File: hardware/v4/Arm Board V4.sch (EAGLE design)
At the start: 35 parts, among them IC1 4503D, IC2 4503D, IC7 7812DT, IC9 7812DT, Q3 Q_LTC490, U2 XBEE-1B3

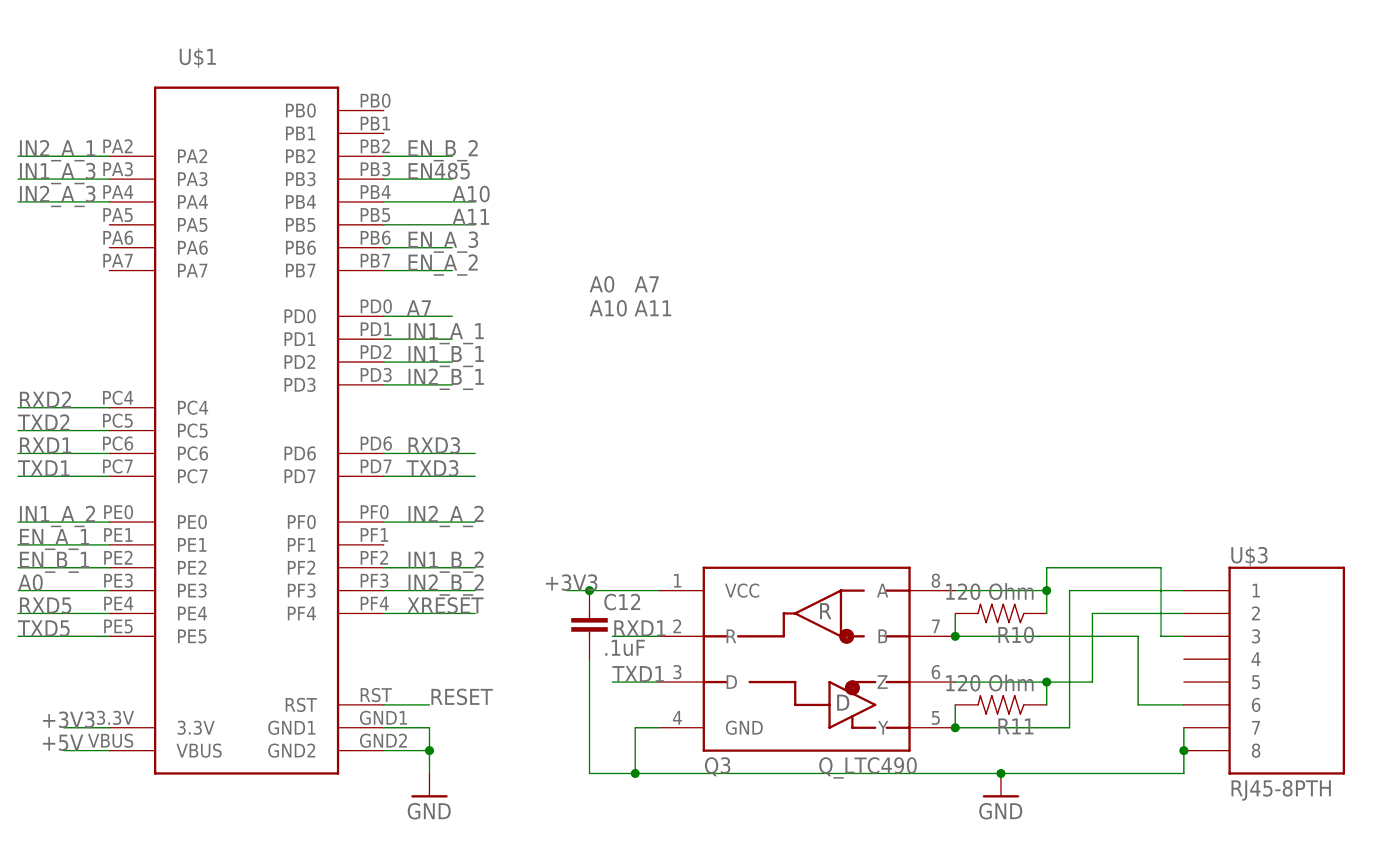
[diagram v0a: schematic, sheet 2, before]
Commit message: Continued work on V4
Started to route power and fixed inconsistency
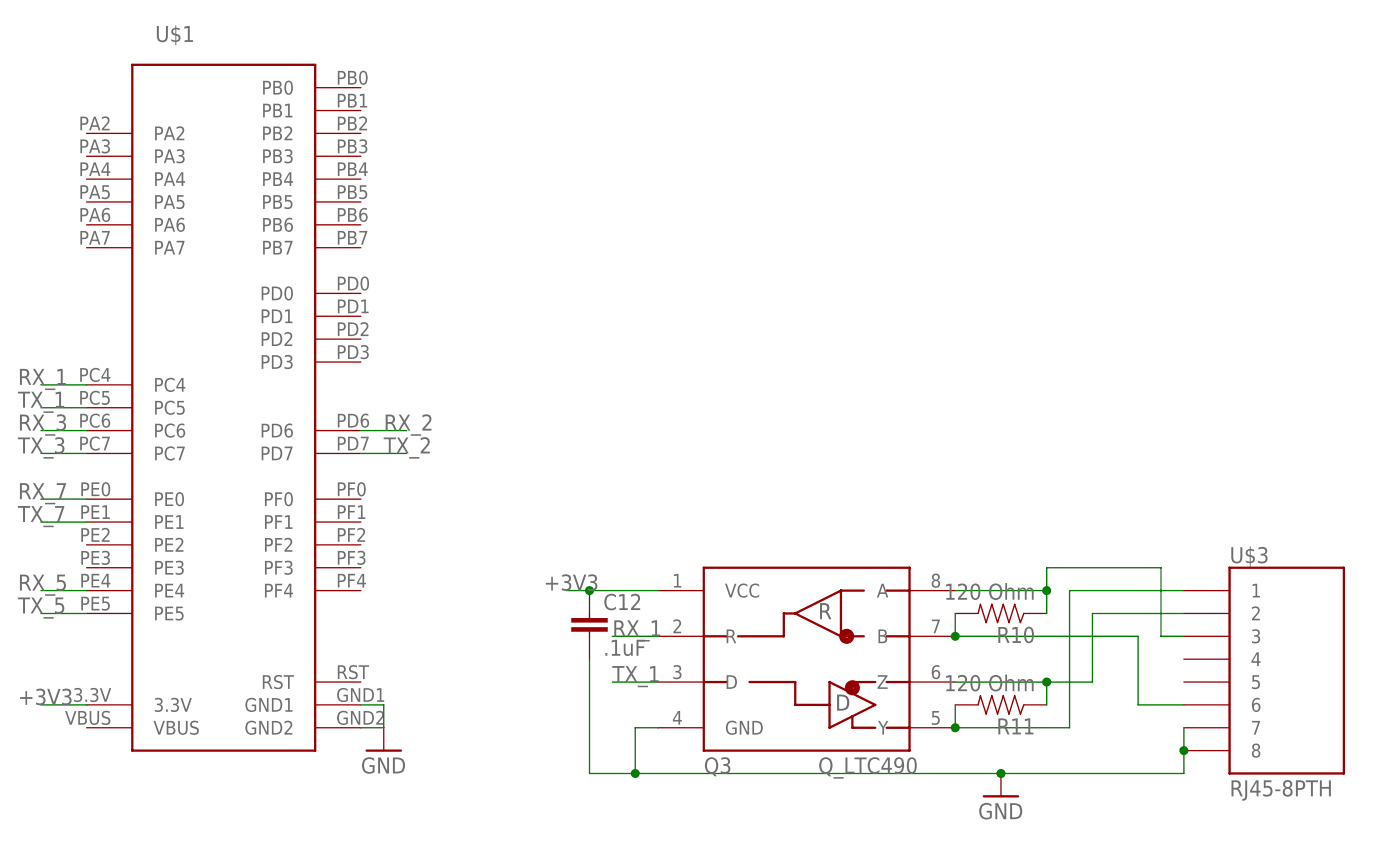
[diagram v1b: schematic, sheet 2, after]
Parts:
- C12: device SparkFun-Capacitors:0.1UF-25V-5%(0603) -> SparkFun-Capacitors:2.2UF-CERCAP-10009
- C20, C21, C22, C23: value 0.1uF -> .1uF; device SparkFun-Capacitors:0.1UF-25V(+80/-20%)(0603) -> SparkFun-Capacitors:2.2UF-CERCAP-10009
- R10, R11: device SparkFun-Passives:RESISTOR0603-RES -> SparkFun-Passives:RESISTOR1206
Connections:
- net EN_A_1 renamed TX_7
- net IN1_A_2 renamed RX_7
- net RXD5 renamed RX_5
- net TXD5 renamed TX_5
- removed net A0: U$1.PE3
- removed net A10: U$1.PB4
- removed net A11: U$1.PB5
- removed net A7: U$1.PD0
- removed net EN485: U$1.PB3
- removed net EN_A_2: U$1.PB7
- removed net EN_A_3: U$1.PB6
- removed net EN_B_1: U$1.PE2
- removed net EN_B_2: U$1.PB2
- removed net IN1_A_1: U$1.PD1
- removed net IN1_A_3: U$1.PA3
- removed net IN1_B_1: U$1.PD2
- removed net IN1_B_2: U$1.PF2
- removed net IN2_A_1: U$1.PA2
- removed net IN2_A_2: U$1.PF0
- removed net IN2_A_3: U$1.PA4
- removed net IN2_B_1: U$1.PD3
- removed net IN2_B_2: U$1.PF3
- removed net RESET: U$1.RST
- removed net RXD1: Q3.R, U$1.PC6
- removed net RXD2: U$1.PC4
- removed net TXD1: Q3.D, U$1.PC7
- removed net TXD2: U$1.PC5
- new net RX_1: Q3.R, U$1.PC4
- new net RX_2: U$1.PD6
- new net RX_3: U$1.PC6
- new net TX_1: Q3.D, U$1.PC5
- new net TX_2: U$1.PD7
- new net TX_3: U$1.PC7
- net +5V: no longer U$1.VBUS
- net RXD3: no longer U$1.PD6
- net TXD3: no longer U$1.PD7
- net XRESET: no longer U$1.PF4
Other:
- note removed: "A0 A7 A10 A11"
- moved on the sheet: U$1

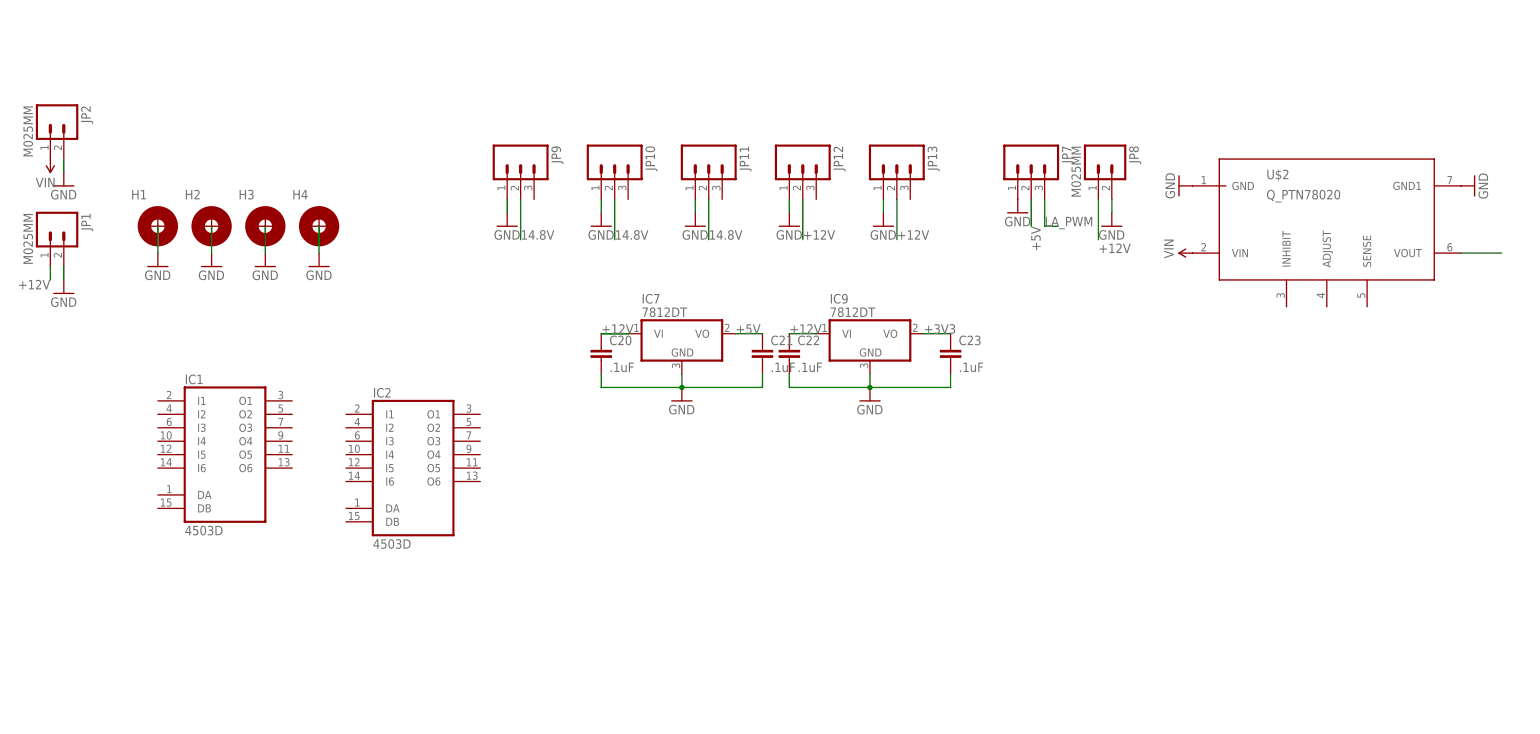
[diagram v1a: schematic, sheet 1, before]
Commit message: Router power and data lines and assigned pins
Started to route more of the data lines to where they will go.  As well
as working on assigning pins to components.
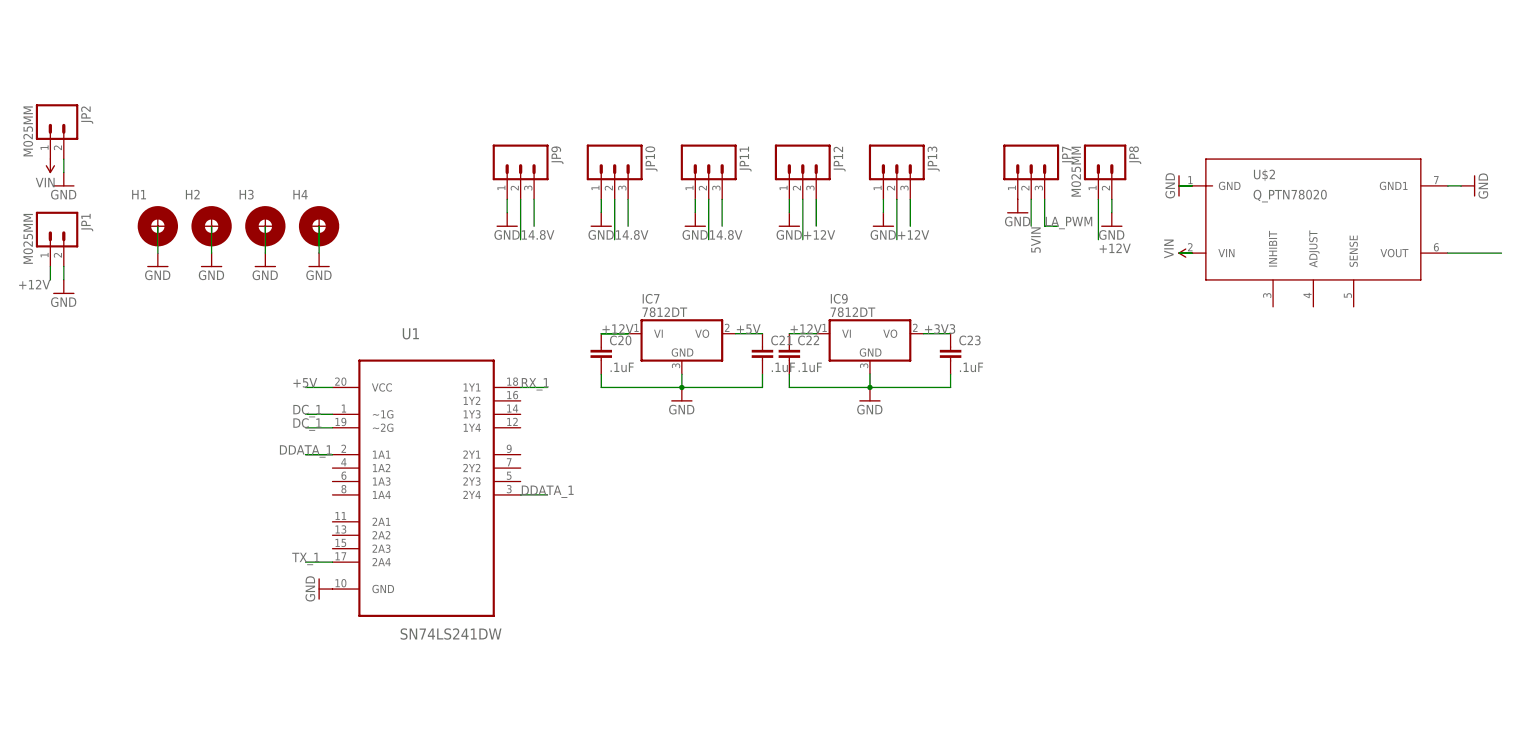
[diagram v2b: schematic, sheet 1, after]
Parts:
- removed IC1, IC2: 4503D, 45xx:4503D
- added U1: SN74LS241DW, 74LS241:SN74LS241DW
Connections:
- removed net RXD3: LED2.C, U2.DOUT
- removed net TXD3: LED3.C, U2.DIN
- new net 5VIN: JP7.2
- new net DC_1: U$1.PB3, U1.~1G, U1.~2G
- new net DDATA_1: JP10.3, JP11.3, JP12.3, JP13.3, JP9.3, U1.1A1, U1.2Y4
- net +5V: now also U1.VCC; no longer JP7.2
- net GND: now also U1.GND
- net LA_PWM: now also U$1.PB6
- net RX_1: now also U1.1Y1; no longer Q3.R
- net RX_2: now also Q3.R
- net RX_3: now also LED2.C, U2.DOUT
- net TX_1: now also U1.2A4; no longer Q3.D
- net TX_2: now also Q3.D
- net TX_3: now also LED3.C, U2.DIN
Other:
- moved on the sheet: U$2

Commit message: Added a few things and cleaned up some stuff
Added a few things from last night but mostly cleaning up traces and
adding parts to it.  Commit message last night was by Seto so ignore the
message.
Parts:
- added JP4, JP5: (no value), SparkFun-Connectors:M041X04_NO_SILK
- added Q1, Q2, Q4: MOSFET-NCHANNELFQP30N06L, SparkFun-DiscreteSemi:MOSFET-NCHANNELFQP30N06L
- added R3, R6, R7: 150, SparkFun-Passives:RESISTOR1206
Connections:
- new net O1: JP4.2, JP5.2, Q1.D
- new net O2: JP4.3, JP5.3, Q2.D
- new net O3: JP4.4, JP5.4, Q4.D
- new net PWM1: Q1.G, R3.2, U$1.PD1
- new net PWM2: Q2.G, R6.2, U$1.PD2
- new net PWM3: Q4.G, R7.2, U$1.PD3
- net +12V: now also JP4.1, JP5.1
- net GND: now also Q1.S, Q2.S, Q4.S, R3.1, R6.1, R7.1
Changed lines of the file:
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@@
 <part name="U1" library="74LS241" deviceset="SN74LS241DW" device=""/>
 <part name="GND18" library="SparkFun-Aesthetics" deviceset="GND" device=""/>
+<part name="Q1" library="SparkFun-DiscreteSemi" deviceset="MOSFET-NCHANNEL" device="FQP30N06L"/>
+<part name="R3" library="SparkFun-Passives" deviceset="RESISTOR" device="1206" value="150"/>
+<part name="U$4" library="Lib_Documentation" deviceset="SUP_GND" device=""/>
+<part name="Q2" library="SparkFun-DiscreteSemi" deviceset="MOSFET-NCHANNEL" device="FQP30N06L"/>
+<part name="R6" library="SparkFun-Passives" deviceset="RESISTOR" device="1206" value="150"/>
+<part name="U$5" library="Lib_Documentation" deviceset="SUP_GND" device=""/>
+<part name="Q4" library="SparkFun-DiscreteSemi" deviceset="MOSFET-NCHANNEL" device="FQP30N06L"/>
+<part name="R7" library="SparkFun-Passives" deviceset="RESISTOR" device="1206" value="150"/>
+<part name="U$6" library="Lib_Documentation" deviceset="SUP_GND" device=""/>
+<part name="JP4" library="SparkFun-Connectors" deviceset="M04" device="1X04_NO_SILK"/>
+<part name="JP5" library="SparkFun-Connectors" deviceset="M04" device="1X04_NO_SILK"/>
 </parts>
 <sheets>
@@
 <instance part="U1" gate="A" x="76.2" y="-7.62"/>
 <instance part="GND18" gate="1" x="55.88" y="-30.48" rot="R270"/>
+<instance part="Q1" gate="G$1" x="208.28" y="0"/>
+<instance part="R3" gate="G$1" x="195.58" y="-5.08" rot="R90"/>
+<instance part="U$4" gate="G$1" x="200.66" y="-5.08" rot="R180"/>
+<instance part="Q2" gate="G$1" x="208.28" y="-22.86"/>
+<instance part="R6" gate="G$1" x="195.58" y="-27.94" rot="R90"/>
+<instance part="U$5" gate="G$1" x="200.66" y="-27.94" rot="R180"/>
+<instance part="Q4" gate="G$1" x="208.28" y="-45.72"/>
+<instance part="R7" gate="G$1" x="195.58" y="-50.8" rot="R90"/>
+<instance part="U$6" gate="G$1" x="200.66" y="-50.8" rot="R180"/>
+<instance part="JP4" gate="G$1" x="279.4" y="-2.54" rot="R180"/>
+<instance part="JP5" gate="G$1" x="279.4" y="-22.86" rot="R180"/>
 </instances>
 <busses>
@@
 <pinref part="GND18" gate="1" pin="GND"/>
 </segment>
+<segment>
+<pinref part="R3" gate="G$1" pin="1"/>
+<pinref part="Q1" gate="G$1" pin="S"/>
+<wire x1="208.28" y1="-5.08" x2="208.28" y2="-10.16" width="0.1524" layer="91"/>
+<wire x1="208.28" y1="-10.16" x2="200.66" y2="-10.16" width="0.1524" layer="91"/>
+<pinref part="U$4" gate="G$1" pin="GND"/>
+<wire x1="200.66" y1="-10.16" x2="195.58" y2="-10.16" width="0.1524" layer="91"/>
+<wire x1="200.66" y1="-7.62" x2="200.66" y2="-10.16" width="0.1524" layer="91"/>
+</segment>
+<segment>
+<pinref part="R6" gate="G$1" pin="1"/>
+<pinref part="Q2" gate="G$1" pin="S"/>
+<wire x1="208.28" y1="-27.94" x2="208.28" y2="-33.02" width="0.1524" layer="91"/>
+<wire x1="208.28" y1="-33.02" x2="200.66" y2="-33.02" width="0.1524" layer="91"/>
+<pinref part="U$5" gate="G$1" pin="GND"/>
+<wire x1="200.66" y1="-33.02" x2="195.58" y2="-33.02" width="0.1524" layer="91"/>
+<wire x1="200.66" y1="-30.48" x2="200.66" y2="-33.02" width="0.1524" layer="91"/>
+</segment>
+<segment>
+<pinref part="R7" gate="G$1" pin="1"/>
+<pinref part="Q4" gate="G$1" pin="S"/>
+<wire x1="208.28" y1="-50.8" x2="208.28" y2="-55.88" width="0.1524" layer="91"/>
+<wire x1="208.28" y1="-55.88" x2="200.66" y2="-55.88" width="0.1524" layer="91"/>
+<pinref part="U$6" gate="G$1" pin="GND"/>
+<wire x1="200.66" y1="-55.88" x2="195.58" y2="-55.88" width="0.1524" layer="91"/>
+<wire x1="200.66" y1="-53.34" x2="200.66" y2="-55.88" width="0.1524" layer="91"/>
+</segment>
 </net>
 <net name="+12V" class="0">
@@
 <pinref part="JP12" gate="G$1" pin="2"/>
 </segment>
+<segment>
+<pinref part="JP4" gate="G$1" pin="1"/>
+<wire x1="274.32" y1="0" x2="269.24" y2="0" width="0.1524" layer="91"/>
+<label x="269.24" y="0" size="1.778" layer="95"/>
+</segment>
+<segment>
+<pinref part="JP5" gate="G$1" pin="1"/>
+<wire x1="274.32" y1="-20.32" x2="269.24" y2="-20.32" width="0.1524" layer="91"/>
+<label x="269.24" y="-20.32" size="1.778" layer="95"/>
+</segment>
 </net>
 <net name="+5V" class="0">
@@
 <wire x1="58.42" y1="-25.4" x2="53.34" y2="-25.4" width="0.1524" layer="91"/>
 <label x="50.8" y="-25.4" size="1.778" layer="95"/>
+</segment>
+</net>
+<net name="O1" class="0">
+<segment>
+<pinref part="Q1" gate="G$1" pin="D"/>
+<wire x1="208.28" y1="5.08" x2="208.28" y2="10.16" width="0.1524" layer="91"/>
+<label x="208.28" y="10.16" size="1.778" layer="95"/>
+</segment>
+<segment>
+<pinref part="JP4" gate="G$1" pin="2"/>
+<wire x1="274.32" y1="-2.54" x2="269.24" y2="-2.54" width="0.1524" layer="91"/>
+<label x="269.24" y="-2.54" size="1.778" layer="95"/>
+</segment>
+<segment>
+<pinref part="JP5" gate="G$1" pin="2"/>
+<wire x1="274.32" y1="-22.86" x2="269.24" y2="-22.86" width="0.1524" layer="91"/>
+<label x="269.24" y="-22.86" size="1.778" layer="95"/>
+</segment>
+</net>
+<net name="PWM1" class="0">
+<segment>
+<pinref part="Q1" gate="G$1" pin="G"/>
+<pinref part="R3" gate="G$1" pin="2"/>
+<wire x1="200.66" y1="0" x2="195.58" y2="0" width="0.1524" layer="91"/>
+<wire x1="187.96" y1="0" x2="195.58" y2="0" width="0.1524" layer="91"/>
+<label x="187.96" y="0" size="1.778" layer="95"/>
+</segment>
+</net>
+<net name="PWM2" class="0">
+<segment>
+<pinref part="Q2" gate="G$1" pin="G"/>
+<pinref part="R6" gate="G$1" pin="2"/>
+<wire x1="200.66" y1="-22.86" x2="195.58" y2="-22.86" width="0.1524" layer="91"/>
+<wire x1="187.96" y1="-22.86" x2="195.58" y2="-22.86" width="0.1524" layer="91"/>
+<label x="187.96" y="-22.86" size="1.778" layer="95"/>
+</segment>
+</net>
+<net name="PWM3" class="0">
+<segment>
+<pinref part="Q4" gate="G$1" pin="G"/>
+<pinref part="R7" gate="G$1" pin="2"/>
+<wire x1="200.66" y1="-45.72" x2="195.58" y2="-45.72" width="0.1524" layer="91"/>
+<wire x1="187.96" y1="-45.72" x2="195.58" y2="-45.72" width="0.1524" layer="91"/>
+<label x="187.96" y="-45.72" size="1.778" layer="95"/>
+</segment>
+</net>
+<net name="O2" class="0">
+<segment>
+<pinref part="Q2" gate="G$1" pin="D"/>
+<wire x1="208.28" y1="-17.78" x2="208.28" y2="-12.7" width="0.1524" layer="91"/>
+<label x="208.28" y="-12.7" size="1.778" layer="95"/>
+</segment>
+<segment>
+<pinref part="JP4" gate="G$1" pin="3"/>
+<wire x1="274.32" y1="-5.08" x2="269.24" y2="-5.08" width="0.1524" layer="91"/>
+<label x="269.24" y="-5.08" size="1.778" layer="95"/>
+</segment>
+<segment>
+<pinref part="JP5" gate="G$1" pin="3"/>
+<wire x1="274.32" y1="-25.4" x2="269.24" y2="-25.4" width="0.1524" layer="91"/>
+<label x="269.24" y="-25.4" size="1.778" layer="95"/>
+</segment>
+</net>
+<net name="O3" class="0">
+<segment>
+<pinref part="Q4" gate="G$1" pin="D"/>
+<wire x1="208.28" y1="-40.64" x2="208.28" y2="-35.56" width="0.1524" layer="91"/>
+<label x="208.28" y="-35.56" size="1.778" layer="95"/>
+</segment>
+<segment>
+<pinref part="JP4" gate="G$1" pin="4"/>
+<wire x1="274.32" y1="-7.62" x2="269.24" y2="-7.62" width="0.1524" layer="91"/>
+<label x="269.24" y="-7.62" size="1.778" layer="95"/>
+</segment>
+<segment>
+<pinref part="JP5" gate="G$1" pin="4"/>
+<wire x1="274.32" y1="-27.94" x2="269.24" y2="-27.94" width="0.1524" layer="91"/>
+<label x="269.24" y="-27.94" size="1.778" layer="95"/>
 </segment>
 </net>
@@
 </segment>
 </net>
+<net name="PWM3" class="0">
+<segment>
+<pinref part="U$1" gate="G$1" pin="PD3"/>
+<wire x1="40.64" y1="48.26" x2="45.72" y2="48.26" width="0.1524" layer="91"/>
+</segment>
+</net>
+<net name="PWM2" class="0">
+<segment>
+<pinref part="U$1" gate="G$1" pin="PD2"/>
+<wire x1="40.64" y1="50.8" x2="45.72" y2="50.8" width="0.1524" layer="91"/>
+</segment>
+</net>
+<net name="PWM1" class="0">
+<segment>
+<pinref part="U$1" gate="G$1" pin="PD1"/>
+<wire x1="40.64" y1="53.34" x2="45.72" y2="53.34" width="0.1524" layer="91"/>
+</segment>
+</net>
